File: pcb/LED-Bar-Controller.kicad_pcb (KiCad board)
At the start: 4 copper layers, 46 x 44 mm, 39 parts, among them J1 Conn_01x03, J2 USB_C, J3 Serial, Q1 AO3400A, Q2 AO3400A, SW1 Power, SW2 Color, SW3 Bright-, SW4 Bright+, U1 ESP32-WROOM-32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

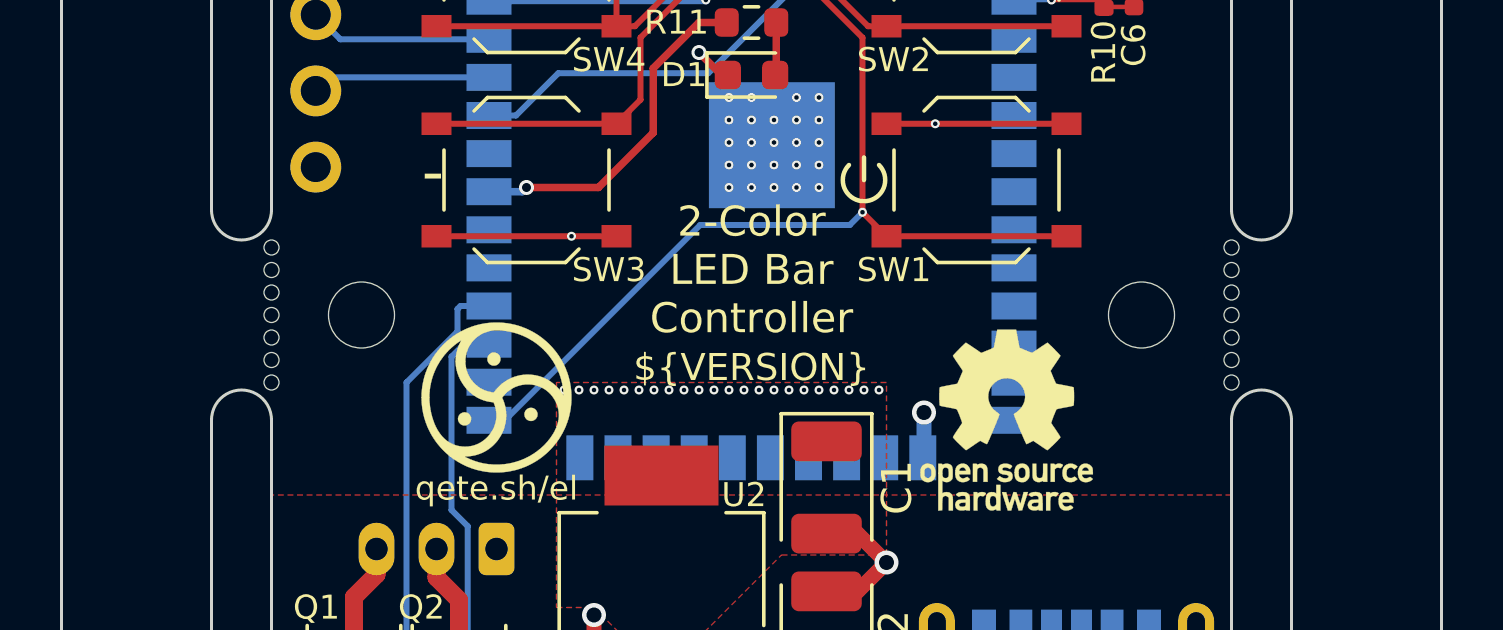
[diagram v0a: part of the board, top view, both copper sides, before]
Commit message: feat: add mouse bites
Add more mouse bites to make breaking the rails easier
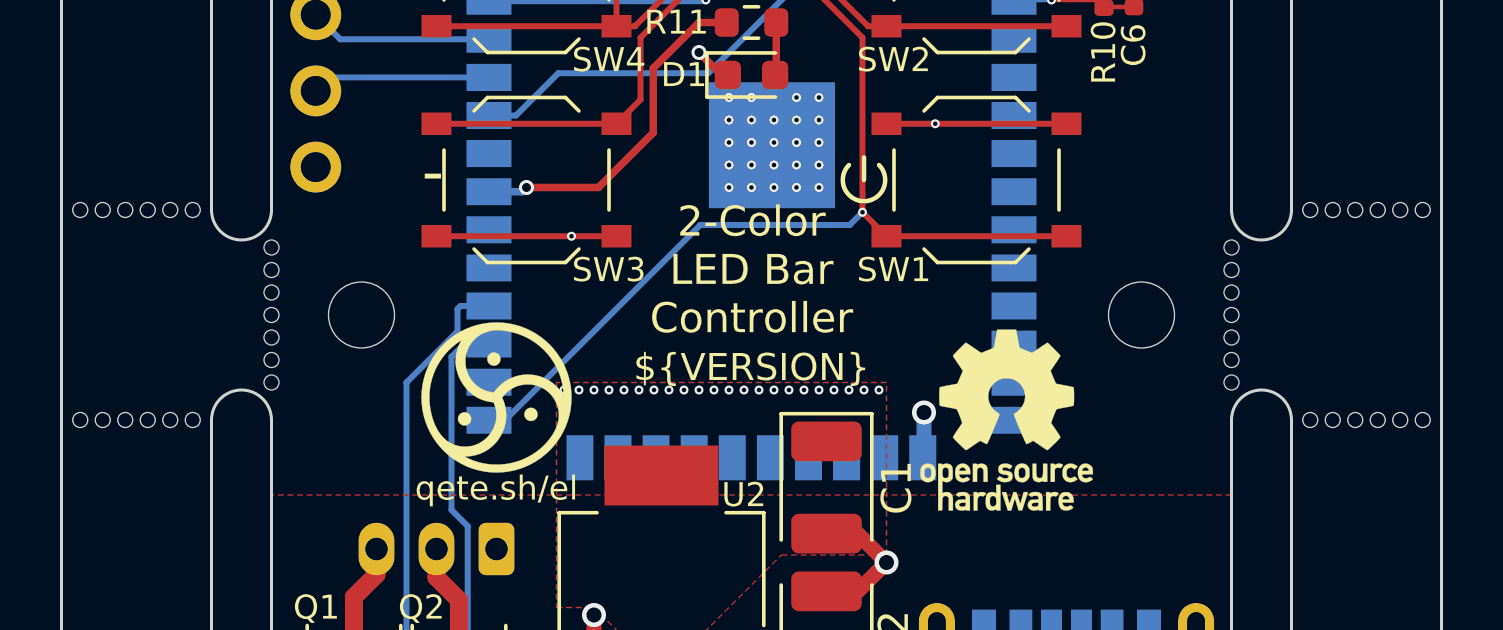
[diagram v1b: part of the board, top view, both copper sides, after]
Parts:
- added mouse-bite-2mm-slot: VAL**, Panelization:mouse-bite-5mm-railbreaker, F.Cu at (118.2, 96.5)
- added mouse-bite-2mm-slot: VAL**, Panelization:mouse-bite-5mm-railbreaker, F.Cu at (159.2, 103.5)
- added mouse-bite-2mm-slot: VAL**, Panelization:mouse-bite-5mm-railbreaker, F.Cu at (159.2, 96.5)
- added mouse-bite-2mm-slot: VAL**, Panelization:mouse-bite-5mm-railbreaker, F.Cu at (118.2, 103.5)
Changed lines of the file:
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@@
     )
+  )
+  (footprint "Panelization:mouse-bite-5mm-railbreaker" (layer "F.Cu")
+    (at 118.25 96.5)
+    (attr board_only exclude_from_pos_files exclude_from_bom allow_missing_courtyard)
+    (fp_text reference "mouse-bite-2mm-slot" (at 0 -1.25) (layer "F.SilkS") hide
+        (effects (font (size 1 1) (thickness 0.2)))
+    )
+    (fp_text value "VAL**" (at 0 2.85) (layer "F.SilkS") hide
+        (effects (font (size 1 1) (thickness 0.2)))
+    )
+    (pad "" np_thru_hole circle (at -1.875 0) (size 0.5 0.5) (drill 0.5) (layers "*.Cu" "*.Mask"))
+    (pad "" np_thru_hole circle (at -1.125 0) (size 0.5 0.5) (drill 0.5) (layers "*.Cu" "*.Mask"))
+    (pad "" np_thru_hole circle (at -0.375 0) (size 0.5 0.5) (drill 0.5) (layers "*.Cu" "*.Mask"))
+    (pad "" np_thru_hole circle (at 0.375 0) (size 0.5 0.5) (drill 0.5) (layers "*.Cu" "*.Mask"))
+    (pad "" np_thru_hole circle (at 1.125 0) (size 0.5 0.5) (drill 0.5) (layers "*.Cu" "*.Mask"))
+    (pad "" np_thru_hole circle (at 1.875 0) (size 0.5 0.5) (drill 0.5) (layers "*.Cu" "*.Mask"))
   )
   (footprint "MountingHole:MountingHole_2.2mm_M2" (layer "F.Cu")
@@
       (rotate (xyz 0 0 0))
     )
+  )
+  (footprint "Panelization:mouse-bite-5mm-railbreaker" (layer "F.Cu")
+    (at 159.25 103.5)
+    (attr board_only exclude_from_pos_files exclude_from_bom allow_missing_courtyard)
+    (fp_text reference "mouse-bite-2mm-slot" (at 0 -1.25) (layer "F.SilkS") hide
+        (effects (font (size 1 1) (thickness 0.2)))
+    )
+    (fp_text value "VAL**" (at 0 2.85) (layer "F.SilkS") hide
+        (effects (font (size 1 1) (thickness 0.2)))
+    )
+    (pad "" np_thru_hole circle (at -1.875 0) (size 0.5 0.5) (drill 0.5) (layers "*.Cu" "*.Mask"))
+    (pad "" np_thru_hole circle (at -1.125 0) (size 0.5 0.5) (drill 0.5) (layers "*.Cu" "*.Mask"))
+    (pad "" np_thru_hole circle (at -0.375 0) (size 0.5 0.5) (drill 0.5) (layers "*.Cu" "*.Mask"))
+    (pad "" np_thru_hole circle (at 0.375 0) (size 0.5 0.5) (drill 0.5) (layers "*.Cu" "*.Mask"))
+    (pad "" np_thru_hole circle (at 1.125 0) (size 0.5 0.5) (drill 0.5) (layers "*.Cu" "*.Mask"))
+    (pad "" np_thru_hole circle (at 1.875 0) (size 0.5 0.5) (drill 0.5) (layers "*.Cu" "*.Mask"))
   )
   (footprint "Resistor_SMD:R_0402_1005Metric" (layer "F.Cu")
@@
     )
   )
+  (footprint "Panelization:mouse-bite-5mm-railbreaker" (layer "F.Cu")
+    (at 159.25 96.5)
+    (attr board_only exclude_from_pos_files exclude_from_bom allow_missing_courtyard)
+    (fp_text reference "mouse-bite-2mm-slot" (at 0 -1.25) (layer "F.SilkS") hide
+        (effects (font (size 1 1) (thickness 0.2)))
+    )
+    (fp_text value "VAL**" (at 0 2.85) (layer "F.SilkS") hide
+        (effects (font (size 1 1) (thickness 0.2)))
+    )
+    (pad "" np_thru_hole circle (at -1.875 0) (size 0.5 0.5) (drill 0.5) (layers "*.Cu" "*.Mask"))
+    (pad "" np_thru_hole circle (at -1.125 0) (size 0.5 0.5) (drill 0.5) (layers "*.Cu" "*.Mask"))
+    (pad "" np_thru_hole circle (at -0.375 0) (size 0.5 0.5) (drill 0.5) (layers "*.Cu" "*.Mask"))
+    (pad "" np_thru_hole circle (at 0.375 0) (size 0.5 0.5) (drill 0.5) (layers "*.Cu" "*.Mask"))
+    (pad "" np_thru_hole circle (at 1.125 0) (size 0.5 0.5) (drill 0.5) (layers "*.Cu" "*.Mask"))
+    (pad "" np_thru_hole circle (at 1.875 0) (size 0.5 0.5) (drill 0.5) (layers "*.Cu" "*.Mask"))
+  )
   (footprint "Button_Switch_SMD:SW_Push_1P1T_XKB_TS-1187A" (layer "F.Cu")
     (at 131.25 95.5 180)
@@
     )
   )
+  (footprint "Panelization:mouse-bite-5mm-railbreaker" (layer "F.Cu")
+    (at 118.25 103.5)
+    (attr board_only exclude_from_pos_files exclude_from_bom allow_missing_courtyard)
+    (fp_text reference "mouse-bite-2mm-slot" (at 0 -1.25) (layer "F.SilkS") hide
+        (effects (font (size 1 1) (thickness 0.2)))
+    )
+    (fp_text value "VAL**" (at 0 2.85) (layer "F.SilkS") hide
+        (effects (font (size 1 1) (thickness 0.2)))
+    )
+    (pad "" np_thru_hole circle (at -1.875 0) (size 0.5 0.5) (drill 0.5) (layers "*.Cu" "*.Mask"))
+    (pad "" np_thru_hole circle (at -1.125 0) (size 0.5 0.5) (drill 0.5) (layers "*.Cu" "*.Mask"))
+    (pad "" np_thru_hole circle (at -0.375 0) (size 0.5 0.5) (drill 0.5) (layers "*.Cu" "*.Mask"))
+    (pad "" np_thru_hole circle (at 0.375 0) (size 0.5 0.5) (drill 0.5) (layers "*.Cu" "*.Mask"))
+    (pad "" np_thru_hole circle (at 1.125 0) (size 0.5 0.5) (drill 0.5) (layers "*.Cu" "*.Mask"))
+    (pad "" np_thru_hole circle (at 1.875 0) (size 0.5 0.5) (drill 0.5) (layers "*.Cu" "*.Mask"))
+  )
   (footprint "My_Footprints:JLCPCB_Tooling_Hole" (layer "F.Cu")
